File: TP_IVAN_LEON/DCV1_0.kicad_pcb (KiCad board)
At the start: 2 copper layers, 86.4 x 55.4 mm, 44 parts, among them J1 Teclado, P1 POWER IN, P2 CONN_02X08, P3 CONN_01X06, P4 POWER_OUT, P5 ANALOG_IN, P6 DIN_5, U1 LM117H, U2 32.768HZ, U3 12MHZ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

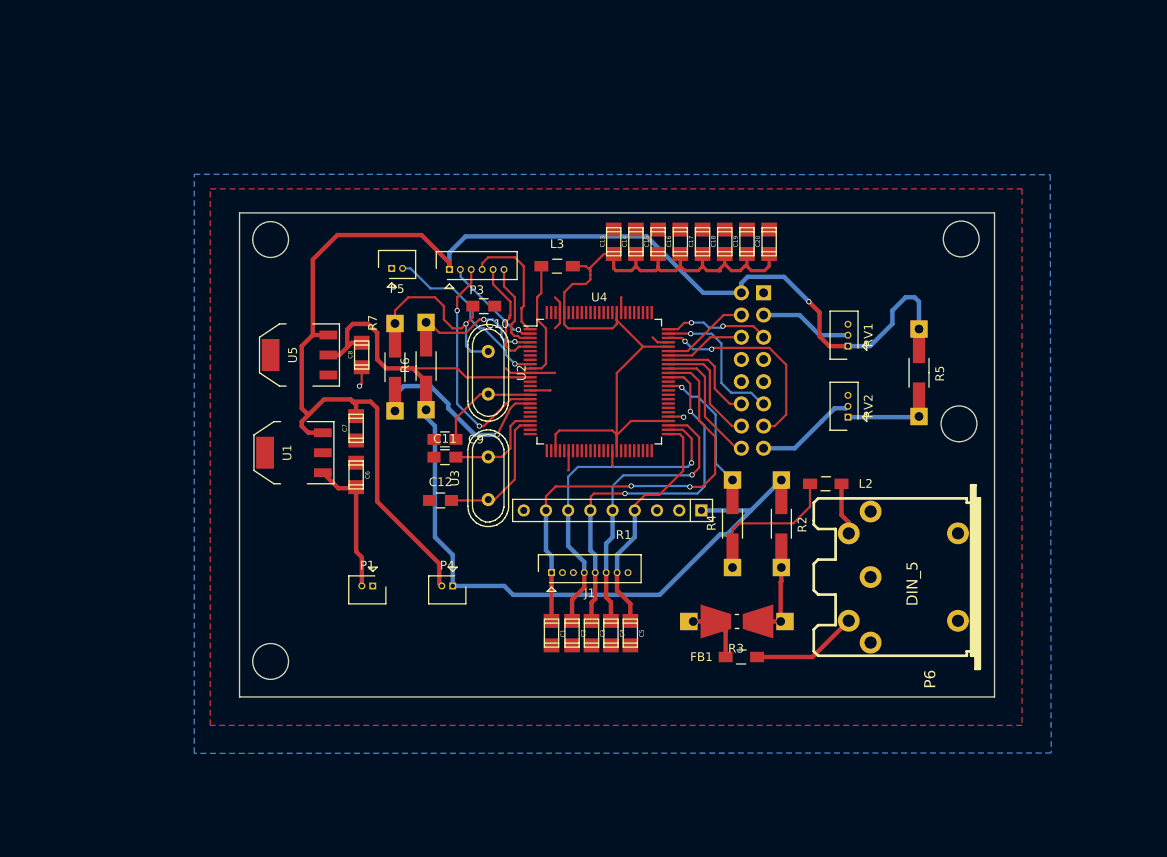
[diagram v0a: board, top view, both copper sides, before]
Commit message: Agregado cambios subrayados en verde descritos en documento Leonv.ods en la carpeta docs
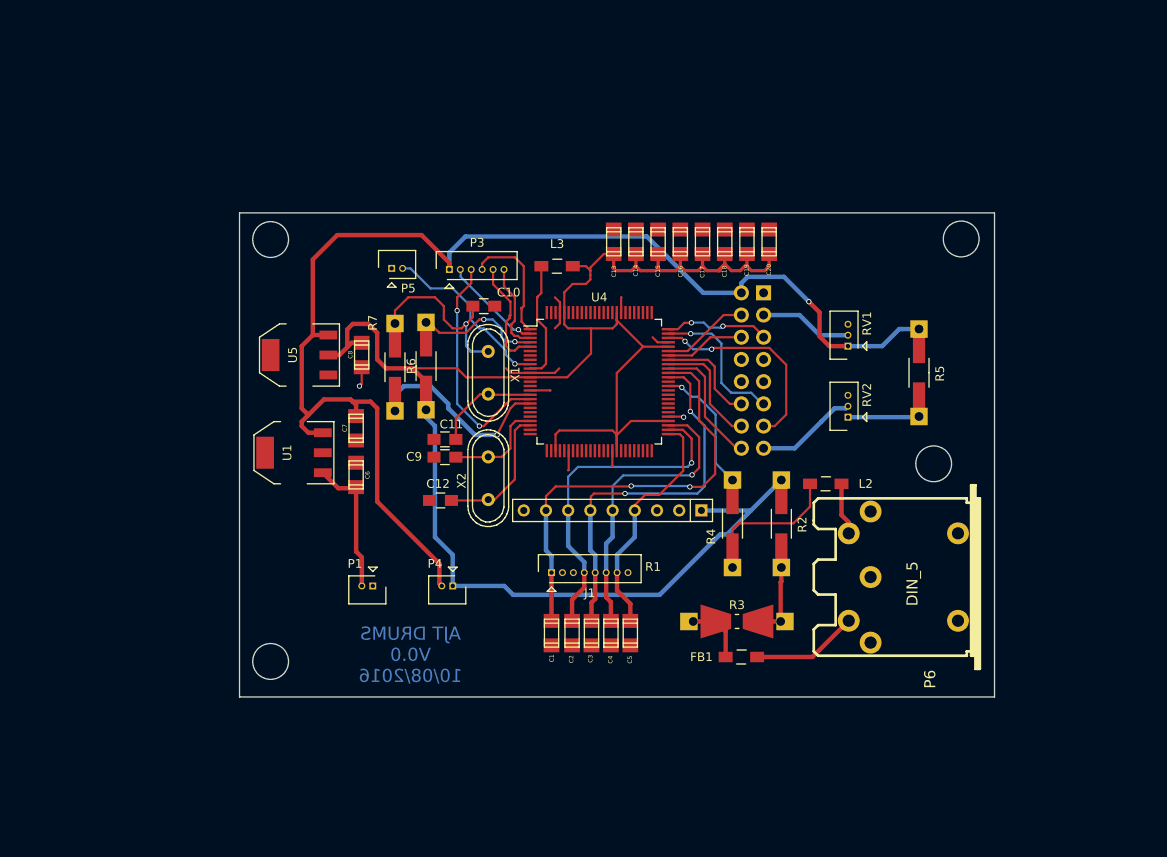
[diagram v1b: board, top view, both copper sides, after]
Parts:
- C11, C12: value 18pF -> 5pF
- C13, C14, C15, C16: value Cap_1206 -> 100nf
- C17, C18, C19, C20: value Cap_1206 -> 10nf
- C6: value Cap_1206 -> 10uf
- C7, C8: value Cap_1206 -> 1uf
- R2: value Res1206 -> 33ohms
- R3: value Res0805 -> 0 ohms
- R4: value Res1206 -> 10 ohms
- R5: value Res1206 -> 220 ohms
- R6: value Res1206 -> 1k ohm
- R7: value Res1206 -> 100k ohms
- U1: value LM117H -> 78L05
- X1: renamed from U2; value 32.768HZ -> 12MHZ
- X2: renamed from U3; value 12MHZ -> 32.768HZ
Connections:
- net /MCU /MIDI_OUT renamed Net-(R4-Pad2)
- net 5V renamed +5V
- C10 pad 2: /MCU /RTCX2 -> Net-(C10-Pad2)
- C11 pad 2: /MCU /XTAL1 -> Net-(C11-Pad2)
- C12 pad 2: /MCU /XTAL2 -> Net-(C12-Pad2)
- C13 pad 2: Net-(C13-Pad2) -> +3V3
- C14 pad 2: Net-(C13-Pad2) -> +3V3
- C15 pad 2: Net-(C13-Pad2) -> +3V3
- C16 pad 2: Net-(C13-Pad2) -> +3V3
- C17 pad 2: Net-(C13-Pad2) -> +3V3
- C18 pad 2: Net-(C13-Pad2) -> +3V3
- C19 pad 2: Net-(C13-Pad2) -> +3V3
- C20 pad 2: Net-(C13-Pad2) -> +3V3
- C8 pad 1: 3.3V -> +3V3
- L3 pad 2: Net-(C13-Pad2) -> +3V3
- P4 pad 1: 3.3V -> +3V3
- R1 pad 1: 3.3V -> +3V3
- R2 pad 1: 3.3V -> +3V3
- R6 pad 1: 3.3V -> +3V3
- R7 pad 1: /MCU /RTCX2 -> Net-(C10-Pad2)
- U4 pad 12: 3.3V -> +3V3
- U4 pad 22: /MCU /XTAL1 -> Net-(C11-Pad2)
- U4 pad 23: /MCU /XTAL2 -> Net-(C12-Pad2)
- U4 pad 28: Net-(C13-Pad2) -> +3V3
- U4 pad 42: Net-(C13-Pad2) -> +3V3
- U4 pad 54: Net-(C13-Pad2) -> +3V3
- U4 pad 71: Net-(C13-Pad2) -> +3V3
- U4 pad 84: Net-(C13-Pad2) -> +3V3
- U4 pad 96: Net-(C13-Pad2) -> +3V3
- U5 pad 2: 3.3V -> +3V3
- X1 pad 1: /MCU /RTCX2 -> Net-(C12-Pad2)
- X1 pad 2: /MCU /RTCX1 -> Net-(C11-Pad2)
- X2 pad 1: /MCU /XTAL2 -> Net-(C10-Pad2)
- X2 pad 2: /MCU /XTAL1 -> /MCU /RTCX1
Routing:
- net +3V3: track 0.00 -> 212.9 mm
- net 3.3V: track 110.2 -> 0.00 mm
- net Net-(C13-Pad2): track 91.7 -> 0.00 mm
- net Net-(C10-Pad2): track 0.00 -> 30.9 mm, vias 0 -> 1
- net /MCU /RTCX2: track 23.2 -> 0.00 mm, vias 1 -> 0
- net /MCU /XTAL2: track 15.8 -> 0.00 mm
- net Net-(C11-Pad2): track 0.00 -> 11.9 mm
- net /MCU /XTAL1: track 11.8 -> 0.00 mm
- net Net-(C12-Pad2): track 0.00 -> 8.14 mm
- net +5V: track 151.6 -> 146.4 mm
- net GND: track 24.3 -> 25.0 mm
- removed copper zone on B.Cu, net GND
- removed copper zone on F.Cu, net GND
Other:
- outline, holes or cut-outs redrawn
- board text added: "AJT DRUMS V0.0 10/08/2016"

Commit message: Agregado fiduciales
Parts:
- added REF**: Fiducial_1mm_Dia_2.54mm_Outer_CopperBottom, TP:Fiducial_1mm_Dia_2.54mm_Outer_CopperBottom, F.Cu at (173.7, 103.5)
- added REF**: Fiducial_1mm_Dia_2.54mm_Outer_CopperTop, TP:Fiducial_1mm_Dia_2.54mm_Outer_CopperTop, F.Cu at (178.3, 79.5)
- added REF**: Fiducial_1mm_Dia_2.54mm_Outer_CopperTop, TP:Fiducial_1mm_Dia_2.54mm_Outer_CopperTop, F.Cu at (111.9, 118.4)
- C1, C2, C3, C4, C5: value Cap_1206 -> 1uf
- C17, C18, C19, C20: value 10nf -> 100nf
- moved C10 15.9 mm to (129.4, 101.3), turned to 0 degrees
- moved C9 15.8 mm to (134.4, 86.4)
- moved X2 12.3 mm to (135.0, 93.7)
- moved X1 11.0 mm to (135.0, 105.0), turned to 90 degrees
- moved C12 0.90 mm to (129.5, 107.7)
- moved C11 0.77 mm to (129.4, 103.5)
- turned C1 to 90 degrees
- turned C2 to 90 degrees
- turned C3 to 90 degrees
- turned C4 to 90 degrees
- turned C5 to 90 degrees
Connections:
- net /MCU /RTCX1 renamed Net-(C9-Pad2)
- C1 pad 1: GND -> /Teclado/BUTTON_ON
- C1 pad 2: /Teclado/BUTTON_ON -> GND
- C2 pad 1: GND -> /Teclado/BUTTON_ENTER
- C2 pad 2: /Teclado/BUTTON_ENTER -> GND
- C3 pad 1: GND -> /Teclado/BUTTON_UP
- C3 pad 2: /Teclado/BUTTON_UP -> GND
- C4 pad 1: GND -> /Teclado/BUTTON_DOWN
- C4 pad 2: /Teclado/BUTTON_DOWN -> GND
- C5 pad 1: GND -> /Teclado/BUTTON_CANCEL
- C5 pad 2: /Teclado/BUTTON_CANCEL -> GND
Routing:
- net Net-(C12-Pad2): track 8.14 -> 15.9 mm
- net Net-(C10-Pad2): track 30.9 -> 26.7 mm
- net Net-(C9-Pad2): track 11.9 -> 13.4 mm, vias 0 -> 1
- added copper zone on B.Cu, net GND
- added copper zone on F.Cu, net GND

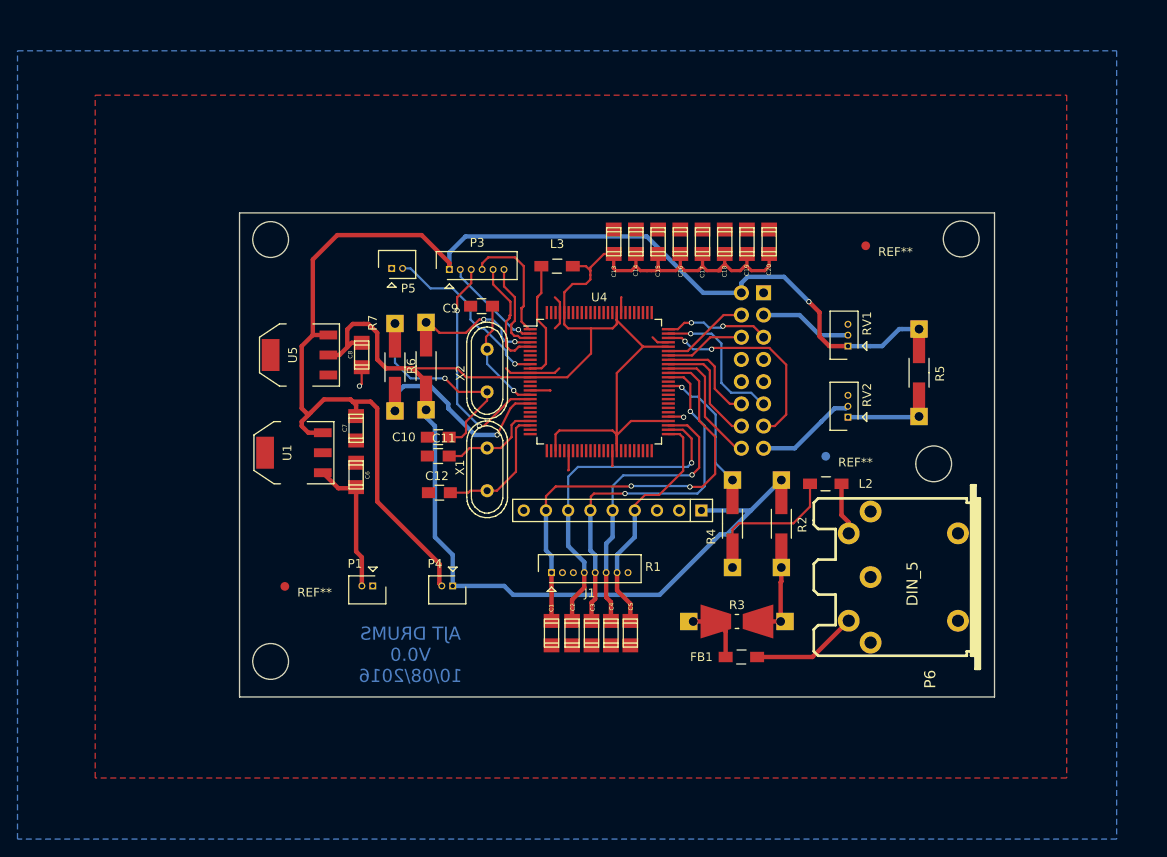
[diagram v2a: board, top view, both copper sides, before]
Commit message: PCB faltante agregado
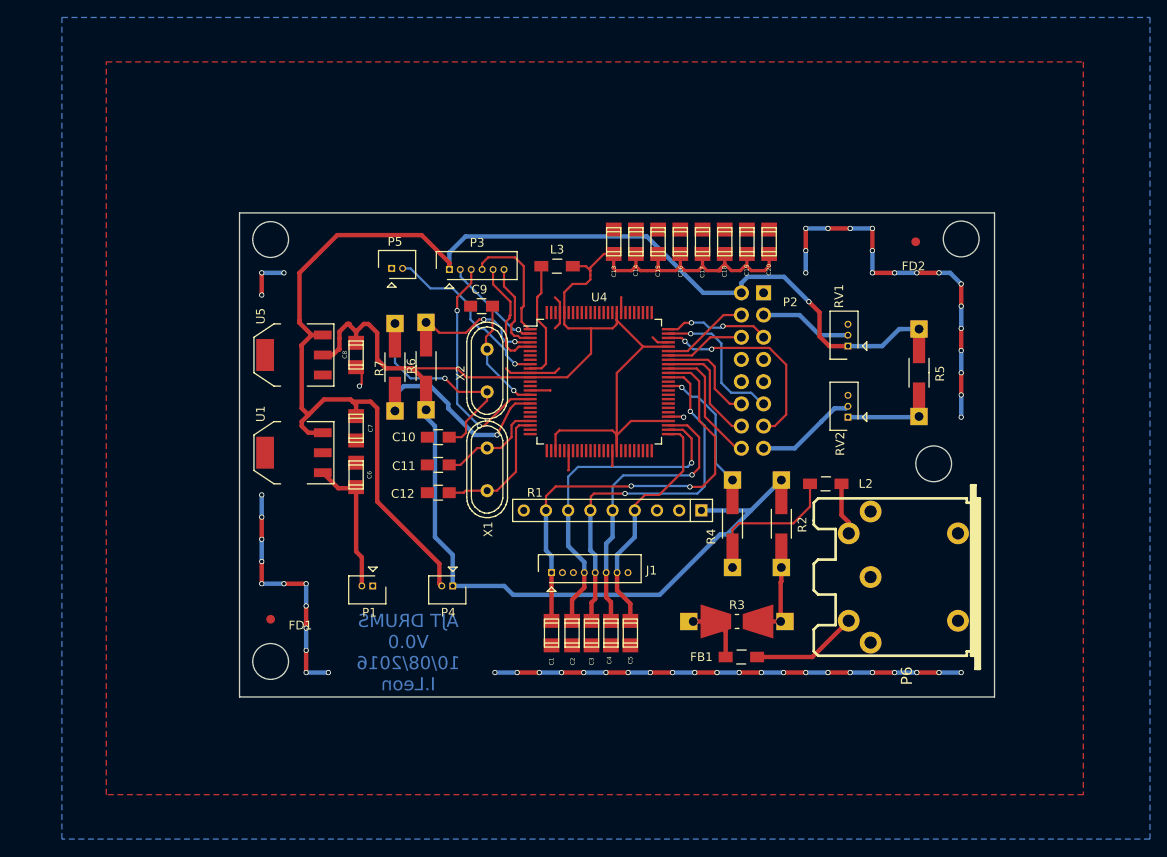
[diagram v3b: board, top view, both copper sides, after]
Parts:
- removed REF**: Fiducial_1mm_Dia_2.54mm_Outer_CopperBottom, TP:Fiducial_1mm_Dia_2.54mm_Outer_CopperBottom
- moved FD2 5.73 mm to (184.0, 79.0)
- moved FD1 4.10 mm to (110.2, 122.2)
- moved C11 1.02 mm to (129.4, 104.5)
- moved C8 0.64 mm to (120.0, 91.9)
- moved U5 0.63 mm to (112.9, 91.9)
- moved C12 0.13 mm to (129.4, 107.7)
- renumbered REF** to FD1, REF** to FD2
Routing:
- net GND: track 25.0 -> 155.1 mm, vias 2 -> 57
- net +5V: track 146.4 -> 147.1 mm
- net +3V3: track 212.9 -> 213.5 mm
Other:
- board text added: "AJT DRUMS V0.0 10/08/2016 I.Leon"
- board text removed: "AJT DRUMS V0.0 10/08/2016"
